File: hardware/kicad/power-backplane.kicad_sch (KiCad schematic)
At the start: 28 parts, among them P500 P500, P501 P501, P502 P502, P503 P503, P504 P504, P505 P505, P506 P506, P601 P601

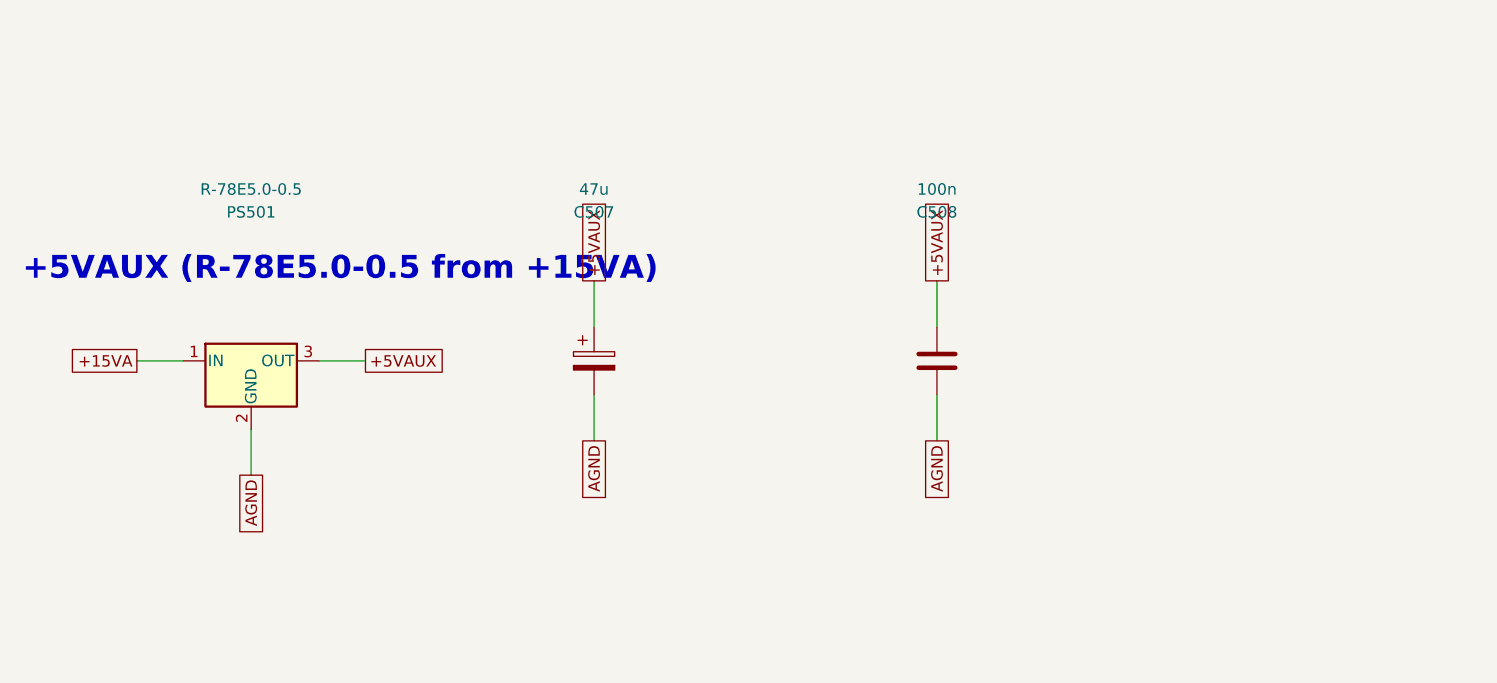
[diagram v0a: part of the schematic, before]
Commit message: Schematic review (kicad-schematic-review skill): F1 R-78E moved to +15VRAW, F2 mono-float bleed R25; both boards re-routed/verified; datasheet cache, per-instance reviews, schematic_review.md
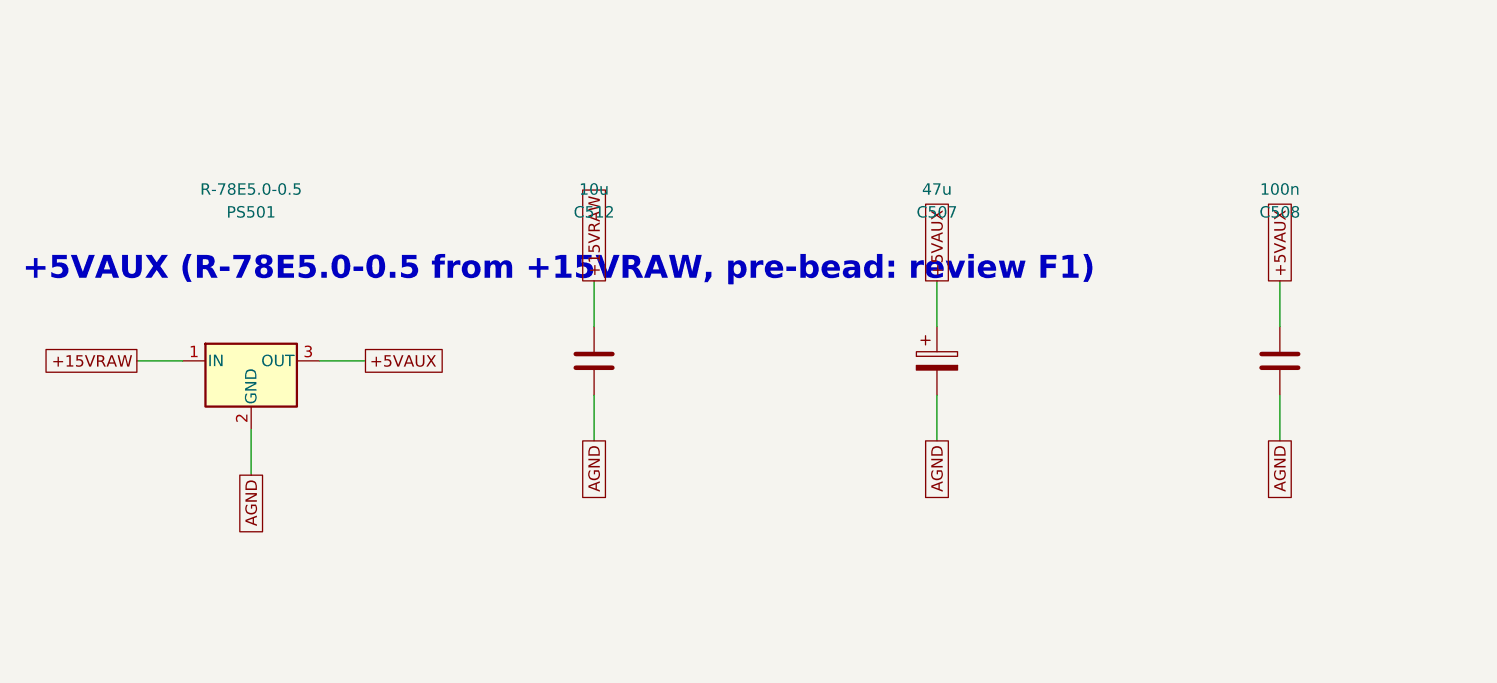
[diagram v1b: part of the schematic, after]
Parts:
- added C508: 100n, Capacitor_SMD:C_0805_2012Metric, symbol Device:C
- C507: renamed from C508; value 100n -> 47u; footprint Capacitor_SMD:C_0805_2012Metric -> Capacitor_THT:CP_Radial_D6.3mm_P2.50mm; symbol Device:C -> Device:C_Polarized; Voltage (none) -> 16V
- C512: renamed from C507; value 47u -> 10u; footprint Capacitor_THT:CP_Radial_D6.3mm_P2.50mm -> Capacitor_SMD:C_1206_3216Metric; symbol Device:C_Polarized -> Device:C; Voltage 16V -> (none)
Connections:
- net +15VA: no longer PS501.1 (IN)
- net +15VRAW: now also C512.1, PS501.1 (IN)
- net +5VAUX: now also C508.1; no longer C512.1
- net AGND: now also C508.2
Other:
- note added: "+5VAUX (R-78E5.0-0.5 from +15VRAW, pre-bead: review F1)"
- note removed: "+5VAUX (R-78E5.0-0.5 from +15VA)"
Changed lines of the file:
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@@
 		)
 	)
-	(text "+5VAUX (R-78E5.0-0.5 from +15VA)"
+	(text "+5VAUX (R-78E5.0-0.5 from +15VRAW, pre-bead: review F1)"
 		(exclude_from_sim yes)
 		(at 25.4 289.56 0)
@@
 	(wire
 		(pts
+			(xy 165.10 295.91) (xy 165.10 290.83)
+		)
+		(stroke
+			(width 0)
+			(type default)
+		)
+	)
+	(wire
+		(pts
+			(xy 165.10 303.53) (xy 165.10 308.61)
+		)
+		(stroke
+			(width 0)
+			(type default)
+		)
+	)
+	(wire
+		(pts
 			(xy 45.72 368.30) (xy 40.64 368.30)
 		)
@@
 		)
 	)
-	(global_label "+15VA"
+	(global_label "+15VRAW"
 		(shape passive)
 		(at 38.10 299.72 180)
@@
 		)
 	)
-	(global_label "+5VAUX"
+	(global_label "+15VRAW"
 		(shape passive)
 		(at 88.90 290.83 90)
@@
 		)
 	)
+	(global_label "+5VAUX"
+		(shape passive)
+		(at 165.10 290.83 90)
+		(fields_autoplaced yes)
+		(effects
+			(font
+				(size 1.27 1.27)
+			)
+			(justify left)
+		)
+		(property "Intersheetrefs" "${INTERSHEET_REFS}"
+			(at 165.10 290.83 0)
+			(effects
+				(font
+					(size 1.27 1.27)
+				)
+				(hide yes)
+			)
+		)
+	)
+	(global_label "AGND"
+		(shape passive)
+		(at 165.10 308.61 270)
+		(fields_autoplaced yes)
+		(effects
+			(font
+				(size 1.27 1.27)
+			)
+			(justify right)
+		)
+		(property "Intersheetrefs" "${INTERSHEET_REFS}"
+			(at 165.10 308.61 0)
+			(effects
+				(font
+					(size 1.27 1.27)
+				)
+				(hide yes)
+			)
+		)
+	)
 	(global_label "+15VA"
 		(shape passive)
@@
 	)
 	(symbol
-		(lib_id "Device:C_Polarized")
+		(lib_id "Device:C")
 		(at 88.90 299.72 0)
 		(unit 1)
@@
 		(dnp no)
 		(fields_autoplaced yes)
-		(property "Reference" "C507"
+		(property "Reference" "C512"
 			(at 88.90 283.21 0)
 			(effects
@@
 			)
 		)
-		(property "Value" "47u"
+		(property "Value" "10u"
 			(at 88.90 280.67 0)
 			(effects
@@
 			)
 		)
-		(property "Footprint" "Capacitor_THT:CP_Radial_D6.3mm_P2.50mm"
+		(property "Footprint" "Capacitor_SMD:C_1206_3216Metric"
 			(at 88.90 278.13 0)
 			(effects
@@
 			)
 		)
+		(pin "1"
+		)
+		(pin "2"
+		)
+		(instances
+			(project "power-backplane"
+				(path "/afb0f8c4-bf37-5c17-978a-b0f2cc7e01bd"
+					(reference "C512")
+					(unit 1)
+				)
+			)
+		)
+	)
+	(symbol
+		(lib_id "Device:C_Polarized")
+		(at 127.00 299.72 0)
+		(unit 1)
+		(exclude_from_sim no)
+		(in_bom yes)
+		(on_board yes)
+		(dnp no)
+		(fields_autoplaced yes)
+		(property "Reference" "C507"
+			(at 127.00 283.21 0)
+			(effects
+				(font
+					(size 1.27 1.27)
+				)
+			)
+		)
+		(property "Value" "47u"
+			(at 127.00 280.67 0)
+			(effects
+				(font
+					(size 1.27 1.27)
+				)
+			)
+		)
+		(property "Footprint" "Capacitor_THT:CP_Radial_D6.3mm_P2.50mm"
+			(at 127.00 278.13 0)
+			(effects
+				(font
+					(size 1.27 1.27)
+				)
+				(hide yes)
+			)
+		)
+		(property "Datasheet" ""
+			(at 127.00 275.59 0)
+			(effects
+				(font
+					(size 1.27 1.27)
+				)
+				(hide yes)
+			)
+		)
 		(property "Voltage" "16V"
-			(at 88.90 273.05 0)
+			(at 127.00 273.05 0)
 			(effects
 				(font
@@
 	(symbol
 		(lib_id "Device:C")
-		(at 127.00 299.72 0)
+		(at 165.10 299.72 0)
 		(unit 1)
 		(exclude_from_sim no)
@@
 		(fields_autoplaced yes)
 		(property "Reference" "C508"
-			(at 127.00 283.21 0)
+			(at 165.10 283.21 0)
 			(effects
 				(font
@@
 		)
 		(property "Value" "100n"
-			(at 127.00 280.67 0)
+			(at 165.10 280.67 0)
 			(effects
 				(font
@@
 		)
 		(property "Footprint" "Capacitor_SMD:C_0805_2012Metric"
-			(at 127.00 278.13 0)
+			(at 165.10 278.13 0)
 			(effects
 				(font
@@
 		)
 		(property "Datasheet" ""
-			(at 127.00 275.59 0)
+			(at 165.10 275.59 0)
 			(effects
 				(font
